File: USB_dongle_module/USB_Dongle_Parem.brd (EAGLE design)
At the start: 40 x 19.2 mm, 25 parts, among them IC3 FT230XS, X1 USB-A, X2 MICROMATCH-6

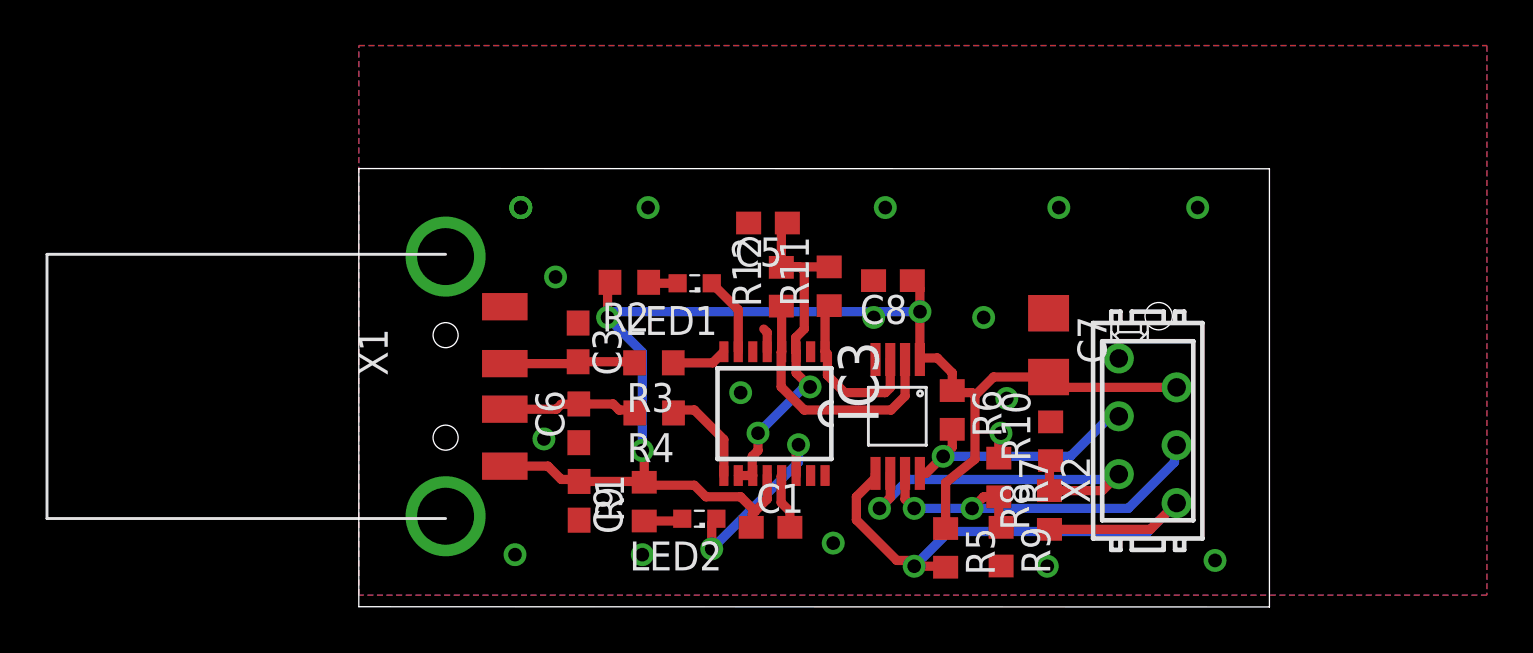
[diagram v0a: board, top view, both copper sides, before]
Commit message: Rerouted USB dongle
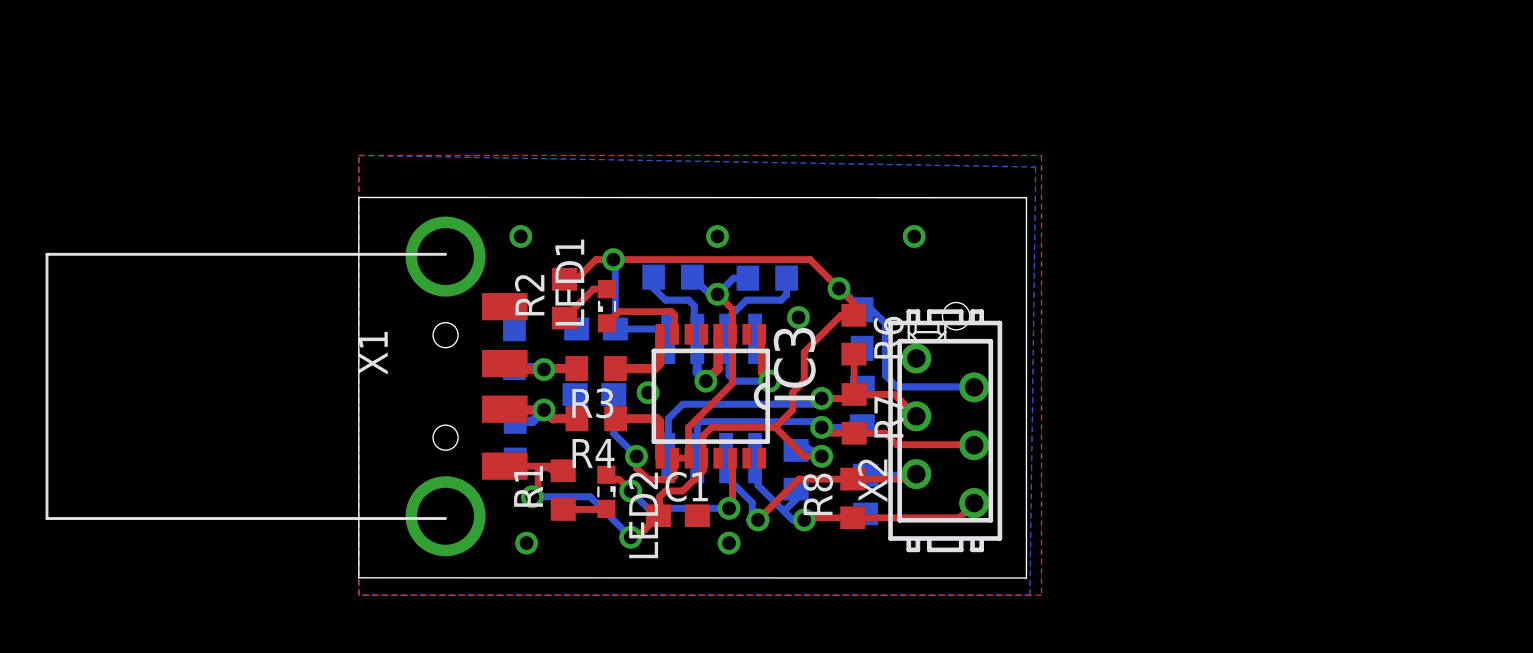
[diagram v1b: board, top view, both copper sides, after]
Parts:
- removed C7: 4,7u, eagle-ltspice:C1206
- removed C8, C9: 100n, eagle-ltspice:C0603
- removed U$2: SN65HVD77D, Kommunikatsioon:SOIC-8
- added C2, C4: 100n, eagle-ltspice:C0603
- added U$1: SN75179BDR, SparkFun-DigitalIC:SOIC8
- moved C5 10.7 mm to (10.3, 8.81), flipped to the bottom, turned to 0 degrees
- moved X2 8.89 mm to (25.7, 7.22)
- moved R9 8.66 mm to (22.1, 8.29), flipped to the bottom, turned to 90 degrees
- moved R8 8.65 mm to (21.7, 4.25)
- moved R10 8.46 mm to (22.2, 4.42), flipped to the bottom, turned to 270 degrees
- moved R5 7.41 mm to (19.2, 5.50), flipped to the bottom
- moved R7 6.94 mm to (21.7, 7.96)
- moved R6 5.44 mm to (21.7, 11.4)
- moved R12 4.77 mm to (13.8, 14.0), flipped to the bottom, turned to 180 degrees
- moved LED2 4.25 mm to (10.9, 4.54), turned to 270 degrees
- moved C1 4.10 mm to (14.0, 3.49)
- moved LED1 3.98 mm to (10.9, 12.7), turned to 90 degrees
- moved R1 3.59 mm to (8.98, 4.61)
- moved R2 2.93 mm to (9.04, 13.0), turned to 90 degrees
- moved C6 2.90 mm to (6.87, 6.78), flipped to the bottom
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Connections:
- net A: now also U$1.8; no longer U$2.8
- net B: now also U$1.7; no longer U$2.7
- net GND: now also C2.1, C4.1, U$1.4; no longer C7.1, C8.2, C9.2, U$2.4
- net RXD: now also U$1.2; no longer U$2.2
- net TXD: now also U$1.3; no longer U$2.3
- net VCC: now also C2.2, C4.2, U$1.1; no longer C7.2, C8.1, C9.1, U$2.1
- net Y: now also U$1.5; no longer U$2.5
- net Z: now also U$1.6; no longer U$2.6
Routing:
- net Y: track 25.9 -> 12.9 mm
- net Z: track 17.5 -> 13.7 mm
- net GND: track 3.50 -> 0.00 mm, vias 17 -> 7
- net RXD: track 11.3 -> 8.38 mm, vias 0 -> 1
- net TXD: track 7.58 -> 10.4 mm, vias 0 -> 1
- net A: track 13.4 -> 15.2 mm, vias 2 -> 1
- net VCCIO: track 16.5 -> 18.3 mm
- net B: track 17.5 -> 15.9 mm, vias 2 -> 1
- net VCC: track 60.7 -> 59.5 mm, vias 3 -> 5
- net SAD: track 5.96 -> 4.81 mm, vias 0 -> 1
- net SA: track 5.75 -> 4.61 mm, vias 0 -> 1
- net N$8: track 1.29 -> 2.39 mm
- net D+: track 2.42 -> 3.33 mm
- net D-: track 4.38 -> 3.60 mm
- net RXLED: track 8.95 -> 8.27 mm
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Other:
- board size 40 x 19.2 mm -> 29.3 x 16.7 mm

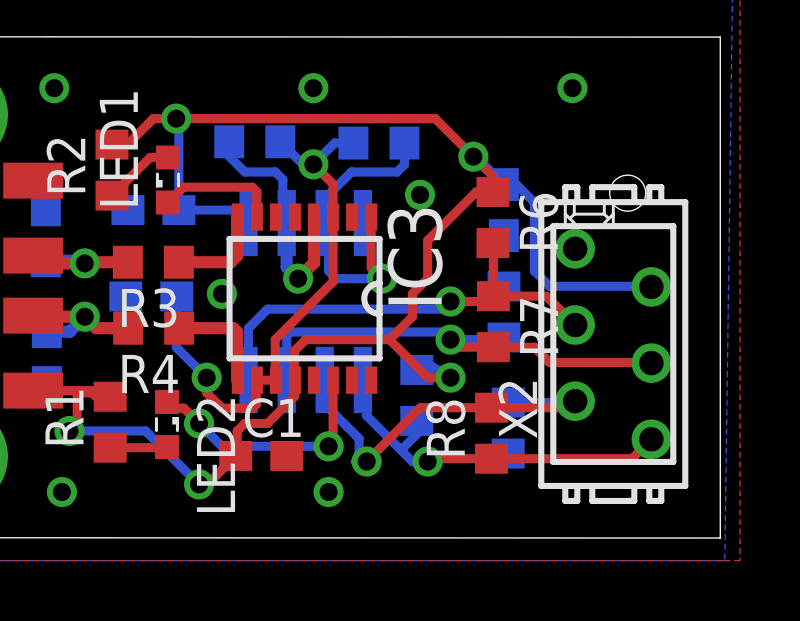
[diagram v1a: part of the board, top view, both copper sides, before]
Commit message: Fixed AB-YZ GND-VCC bugs
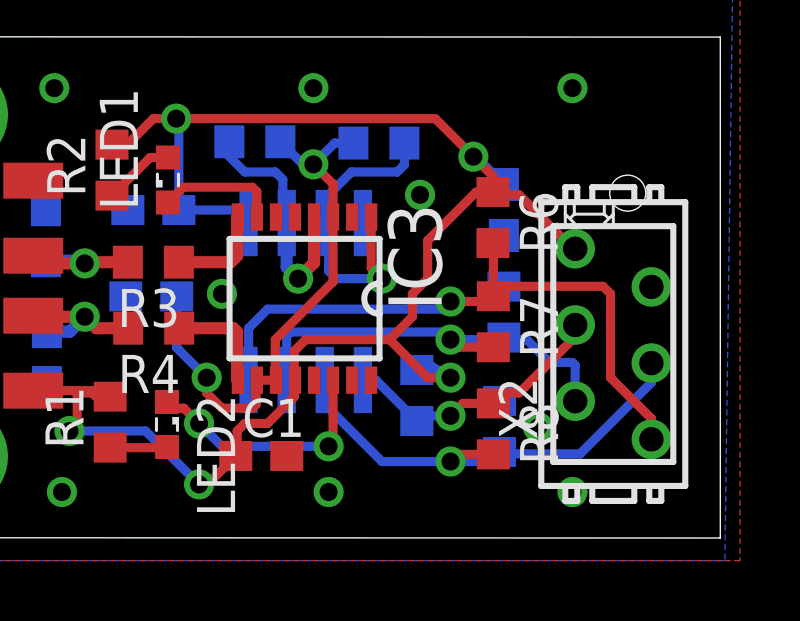
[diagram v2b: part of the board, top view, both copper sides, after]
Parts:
- moved R10 0.30 mm to (22.0, 4.47), turned to 90 degrees
- moved R8 0.16 mm to (21.7, 4.39), turned to 270 degrees
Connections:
- net A: now also X2.6; no longer X2.3
- net B: now also X2.5; no longer X2.4
- net GND: now also X2.2; no longer X2.1
- net VCC: now also X2.1; no longer X2.2
- net Y: now also X2.3; no longer X2.6
- net Z: now also X2.4; no longer X2.5
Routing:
- net A: track 15.2 -> 21.7 mm
- net VCC: track 59.5 -> 55.3 mm
- net Y: track 12.9 -> 9.20 mm
- net Z: track 13.7 -> 15.8 mm
- net B: track 15.9 -> 14.4 mm

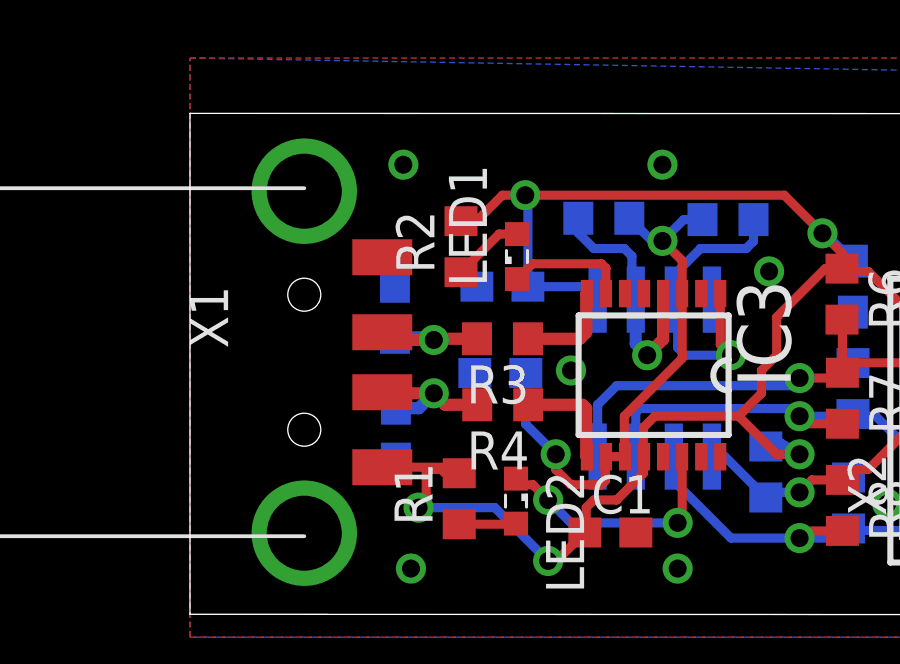
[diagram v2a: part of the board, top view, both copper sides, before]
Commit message: USB D+/D- fixes
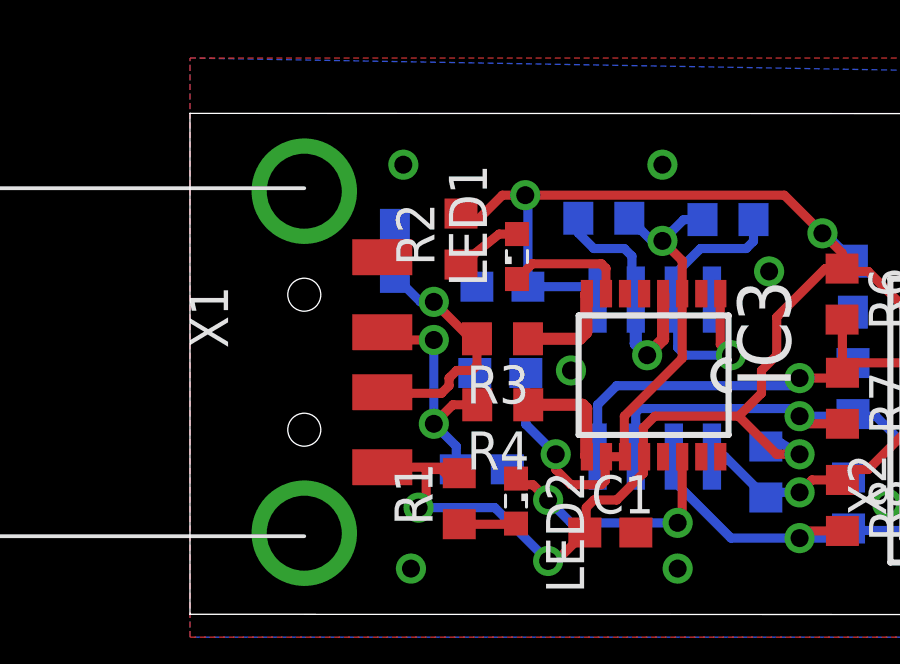
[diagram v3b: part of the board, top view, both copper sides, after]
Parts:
- moved C6 3.10 mm to (9.73, 5.59), turned to 0 degrees
- moved C3 2.03 mm to (6.83, 12.9)
- moved R2 0.25 mm to (9.04, 13.3)
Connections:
- net SA: now also X1.2; no longer X1.3
- net SAD: now also X1.3; no longer X1.2
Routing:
- net SA: track 4.61 -> 8.19 mm
- net SAD: track 4.81 -> 8.16 mm, vias 1 -> 2
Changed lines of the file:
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@@
 </element>
 <element name="R1" library="resistor" package="R0603" value="1000" x="8.976" y="4.614" rot="R90"/>
-<element name="R2" library="resistor" package="R0603" value="1000" x="9.035" y="13.016" rot="R90"/>
+<element name="R2" library="resistor" package="R0603" value="1000" x="9.035" y="13.27" rot="R90"/>
 <element name="IC3" library="ftdichip" package="SSOP16" value="FT230XS" x="15.454" y="8.732" rot="R270"/>
 <element name="C5" library="eagle-ltspice" package="C0603" value="100n" x="10.344" y="8.806" rot="MR0">
@@
 <attribute name="SPICEPREFIX" value="C" x="54.652" y="-33.342" size="1.778" layer="27" display="off"/>
 </element>
-<element name="C3" library="eagle-ltspice" package="C0603" value="47p" x="6.832" y="10.844" rot="MR270">
-<attribute name="SPICEMODEL" value="NONE" x="50.012" y="-36.146" size="1.778" layer="28" rot="MR270" display="off"/>
-<attribute name="SPICEPREFIX" value="C" x="50.012" y="-36.146" size="1.778" layer="28" rot="MR270" display="off"/>
-</element>
-<element name="C6" library="eagle-ltspice" package="C0603" value="47p" x="6.865" y="6.782" rot="MR90">
-<attribute name="SPICEMODEL" value="NONE" x="-41.395" y="23.292" size="1.778" layer="28" rot="MR90" display="off"/>
-<attribute name="SPICEPREFIX" value="C" x="-41.395" y="23.292" size="1.778" layer="28" rot="MR90" display="off"/>
+<element name="C3" library="eagle-ltspice" package="C0603" value="47p" x="6.832" y="12.876" rot="MR270">
+<attribute name="SPICEMODEL" value="NONE" x="50.012" y="-34.114" size="1.778" layer="28" rot="MR270" display="off"/>
+<attribute name="SPICEPREFIX" value="C" x="50.012" y="-34.114" size="1.778" layer="28" rot="MR270" display="off"/>
+</element>
+<element name="C6" library="eagle-ltspice" package="C0603" value="47p" x="9.728" y="5.595" rot="MR0">
+<attribute name="SPICEMODEL" value="NONE" x="-6.782" y="-42.665" size="1.778" layer="28" rot="MR0" display="off"/>
+<attribute name="SPICEPREFIX" value="C" x="-6.782" y="-42.665" size="1.778" layer="28" rot="MR0" display="off"/>
 </element>
 <element name="R5" library="resistor" package="R0603" value="750" x="19.196" y="5.505" rot="MR270"/>
@@
 <wire x1="11.176" y1="14.732" x2="19.812" y2="14.732" width="0.3048" layer="1"/>
 <wire x1="19.812" y1="14.732" x2="21.082" y2="13.462" width="0.3048" layer="1"/>
-<wire x1="9.035" y1="13.866" x2="9.548" y2="13.866" width="0.3048" layer="1"/>
+<wire x1="9.035" y1="14.12" x2="9.548" y2="13.866" width="0.3048" layer="1"/>
 <wire x1="9.548" y1="13.866" x2="10.414" y2="14.732" width="0.3048" layer="1"/>
 <wire x1="10.414" y1="14.732" x2="11.176" y2="14.732" width="0.3048" layer="1"/>
@@
 <contactref element="R2" pad="1"/>
 <wire x1="10.9" y1="13.436" x2="10.305" y2="13.436" width="0.3048" layer="1"/>
-<wire x1="10.305" y1="13.436" x2="9.035" y2="12.166" width="0.3048" layer="1"/>
+<wire x1="10.305" y1="13.436" x2="9.035" y2="12.42" width="0.3048" layer="1"/>
 </signal>
 <signal name="D-">
@@
 </signal>
 <signal name="SA">
-<contactref element="X1" pad="3"/>
 <contactref element="R3" pad="2"/>
 <contactref element="C3" pad="2"/>
-<wire x1="6.832" y1="9.994" x2="8.04" y2="9.994" width="0.4064" layer="16"/>
-<wire x1="8.04" y1="9.994" x2="8.128" y2="9.906" width="0.4064" layer="16"/>
-<via x="8.128" y="9.906" extent="1-16" drill="0.6"/>
-<wire x1="8.128" y1="9.906" x2="6.669" y2="9.906" width="0.4064" layer="1"/>
-<wire x1="6.669" y1="9.906" x2="6.41" y2="10.165" width="0.4064" layer="1"/>
-<wire x1="9.566" y1="9.946" x2="8.168" y2="9.946" width="0.4064" layer="1"/>
-<wire x1="8.168" y1="9.946" x2="8.128" y2="9.906" width="0.4064" layer="1"/>
+<contactref element="X1" pad="2"/>
+<wire x1="9.566" y1="9.946" x2="9.566" y2="9.058" width="0.3048" layer="1"/>
+<wire x1="9.566" y1="9.058" x2="9.398" y2="8.89" width="0.3048" layer="1"/>
+<wire x1="9.398" y1="8.89" x2="8.89" y2="8.89" width="0.3048" layer="1"/>
+<wire x1="8.89" y1="8.89" x2="8.636" y2="8.636" width="0.3048" layer="1"/>
+<wire x1="8.636" y1="8.636" x2="8.636" y2="8.382" width="0.3048" layer="1"/>
+<wire x1="8.636" y1="8.382" x2="8.382" y2="8.128" width="0.3048" layer="1"/>
+<wire x1="8.382" y1="8.128" x2="6.447" y2="8.128" width="0.3048" layer="1"/>
+<wire x1="6.447" y1="8.128" x2="6.41" y2="8.165" width="0.3048" layer="1"/>
+<wire x1="9.566" y1="9.946" x2="9.358" y2="9.946" width="0.3048" layer="1"/>
+<wire x1="9.358" y1="9.946" x2="8.128" y2="11.176" width="0.3048" layer="1"/>
+<via x="8.128" y="11.176" extent="1-16" drill="0.6"/>
+<wire x1="8.128" y1="11.176" x2="7.682" y2="11.176" width="0.3048" layer="16"/>
+<wire x1="7.682" y1="11.176" x2="6.832" y2="12.026" width="0.3048" layer="16"/>
 </signal>
 <signal name="SAD">
 <contactref element="R4" pad="2"/>
 <contactref element="C6" pad="2"/>
-<contactref element="X1" pad="2"/>
-<wire x1="6.865" y1="7.632" x2="7.632" y2="7.632" width="0.4064" layer="16"/>
-<wire x1="7.632" y1="7.632" x2="8.128" y2="8.128" width="0.4064" layer="16"/>
-<via x="8.128" y="8.128" extent="1-16" drill="0.6"/>
-<wire x1="8.128" y1="8.128" x2="6.447" y2="8.128" width="0.4064" layer="1"/>
-<wire x1="6.447" y1="8.128" x2="6.41" y2="8.165" width="0.4064" layer="1"/>
-<wire x1="9.576" y1="7.746" x2="8.51" y2="7.746" width="0.4064" layer="1"/>
-<wire x1="8.51" y1="7.746" x2="8.128" y2="8.128" width="0.4064" layer="1"/>
+<contactref element="X1" pad="3"/>
+<wire x1="9.576" y1="7.746" x2="8.762" y2="7.746" width="0.3048" layer="1"/>
+<wire x1="8.762" y1="7.746" x2="8.128" y2="7.112" width="0.3048" layer="1"/>
+<via x="8.128" y="7.112" extent="1-16" drill="0.6"/>
+<wire x1="8.128" y1="7.112" x2="8.128" y2="9.906" width="0.3048" layer="16"/>
+<via x="8.128" y="9.906" extent="1-16" drill="0.6"/>
+<wire x1="8.128" y1="9.906" x2="6.669" y2="9.906" width="0.3048" layer="1"/>
+<wire x1="6.669" y1="9.906" x2="6.41" y2="10.165" width="0.3048" layer="1"/>
+<wire x1="8.878" y1="5.595" x2="8.878" y2="6.362" width="0.3048" layer="16"/>
+<wire x1="8.878" y1="6.362" x2="8.128" y2="7.112" width="0.3048" layer="16"/>
 </signal>
 </signals>
